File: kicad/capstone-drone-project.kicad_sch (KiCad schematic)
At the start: 0 parts

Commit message: update schematic
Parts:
- added C1, C2: C, symbol Device:C
- added Q1: PMOS, symbol Simulation_SPICE:PMOS
- added R1: 10k, symbol Device:R
- added U1: ESP32-S3, Package_DFN_QFN:QFN-56-1EP_7x7mm_P0.4mm_EP4x4mm, symbol MCU_Espressif:ESP32-S3
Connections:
- new net: Q1.3 (S), R1.1, U1.4 (CHIP_PU)
- new net EN: Q1.2 (G)
- new net GND: C1.2, C2.2, Q1.1 (D), R1.2, U1.57 (GND)
- new net Vcc: C1.1, C2.1, U1.2 (VDD3P3), U1.20 (VDD3P3_RTC), U1.29 (VDD_SPI), U1.3 (VDD3P3), U1.46 (VDD3P3_CPU), U1.55 (VDDA), U1.56 (VDDA)
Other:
- note added: "power supply undetermined but will need voltage regulator"

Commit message: update schematic
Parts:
- added L1: 24n, symbol Device:L
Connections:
- net at U1.54 (XTAL_P): now also L1.2
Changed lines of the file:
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@@
+	)
+	(symbol
+		(lib_id "Device:L")
+		(at 104.14 111.76 90)
+		(unit 1)
+		(exclude_from_sim no)
+		(in_bom yes)
+		(on_board yes)
+		(dnp no)
+		(property "Reference" "L1"
+			(at 104.14 106.68 90)
+			(effects
+				(font
+					(size 1.27 1.27)
+				)
+			)
+		)
+		(property "Value" "24n"
+			(at 104.14 109.22 90)
+			(effects
+				(font
+					(size 1.27 1.27)
+				)
+			)
+		)
+		(property "Footprint" ""
+			(at 104.14 111.76 0)
+			(effects
+				(font
+					(size 1.27 1.27)
+				)
+				(hide yes)
+			)
+		)
+		(property "Datasheet" "~"
+			(at 104.14 111.76 0)
+			(effects
+				(font
+					(size 1.27 1.27)
+				)
+				(hide yes)
+			)
+		)
+		(property "Description" "Inductor"
+			(at 104.14 111.76 0)
+			(effects
+				(font
+					(size 1.27 1.27)
+				)
+				(hide yes)
+			)
+		)
+		(pin "2"
+		)
+		(pin "1"
+		)
+		(instances
+			(project ""
+				(path "/99584293-ff2b-4397-8b8b-c39f1581dc82"
+					(reference "L1")
+					(unit 1)
+				)
+			)
+		)
 	)
 	(symbol

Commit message: working on external clock
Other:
- note added: "maybe use ~26pF capacitors with 18pF,40MHz crystal?"
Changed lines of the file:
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@@
+		)
+	)
+	(text "maybe use ~26pF capacitors with 18pF,40MHz crystal?"
+		(exclude_from_sim no)
+		(at 68.834 104.14 0)
+		(effects
+			(font
+				(size 1.27 1.27)
+			)
 		)
 	)

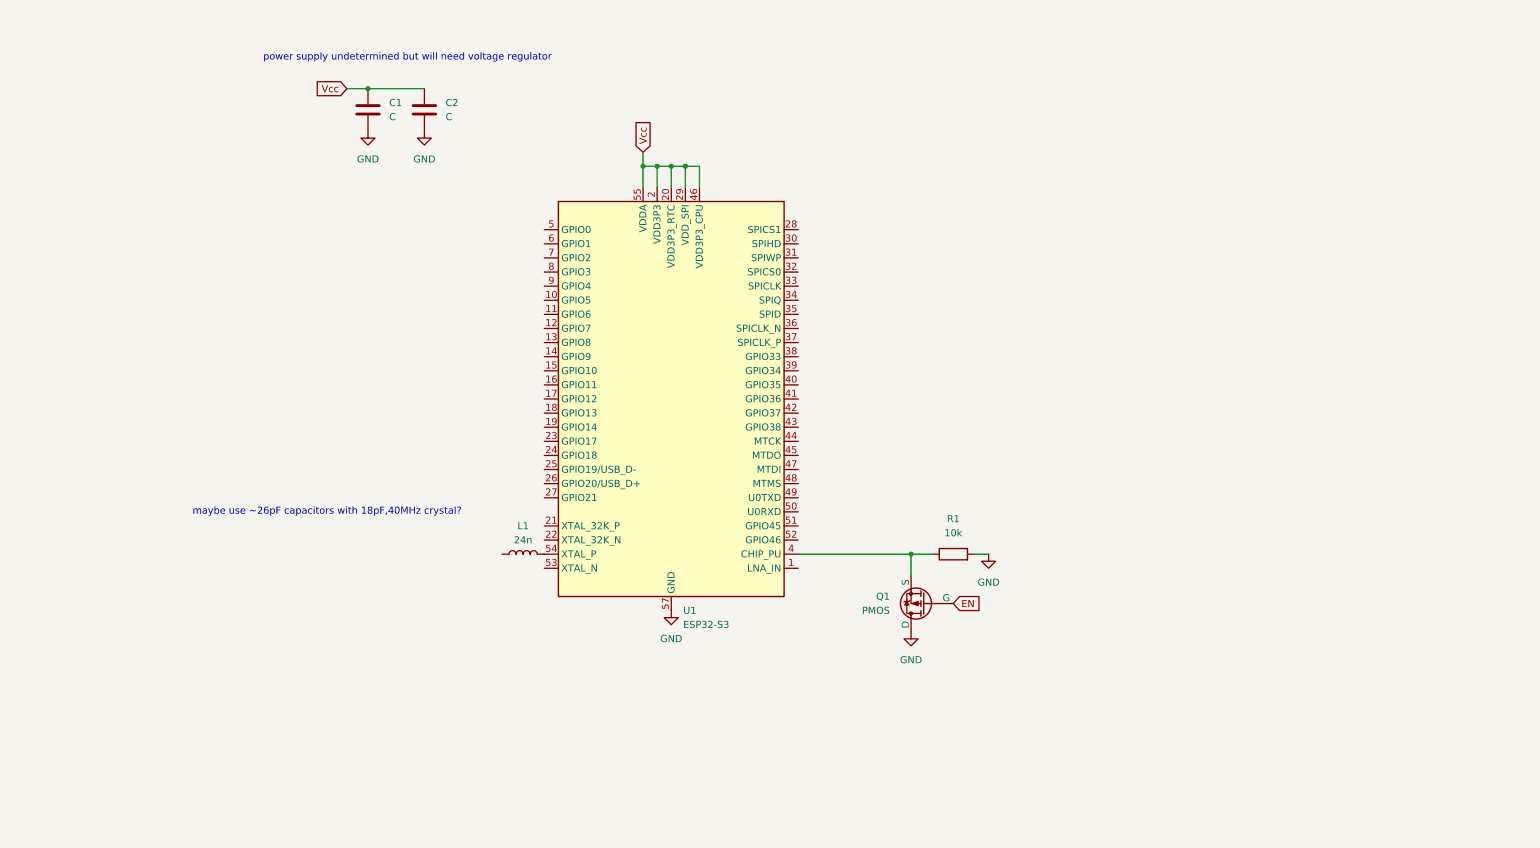
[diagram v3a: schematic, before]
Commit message: added required crystal oscillator and bypass caps
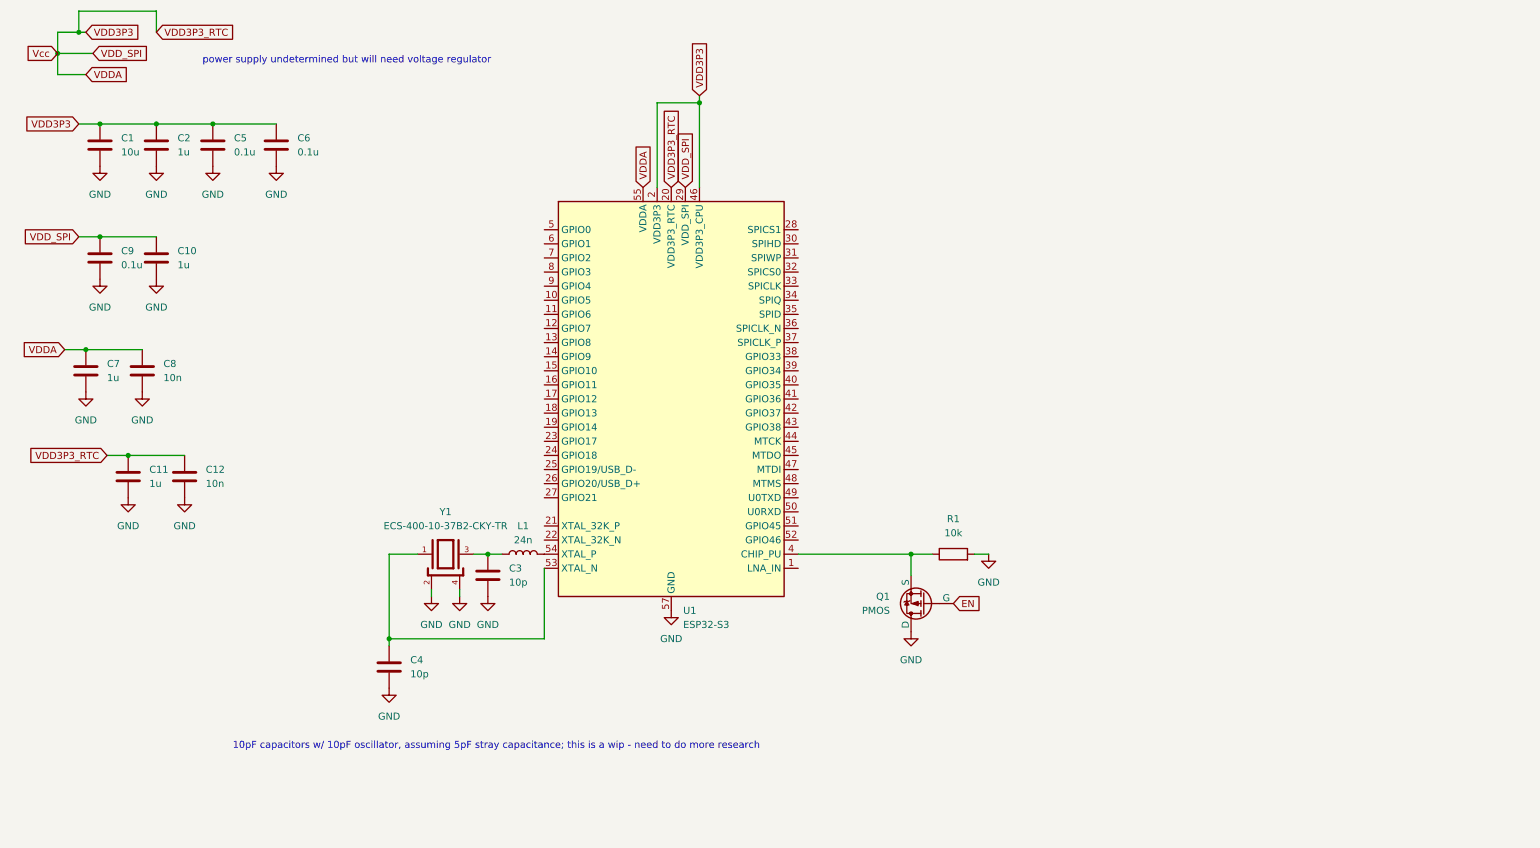
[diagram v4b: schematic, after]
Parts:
- added C10, C11, C7: 1u, symbol Device:C
- added C12, C8: 10n, symbol Device:C
- added C3, C4: 10p, symbol Device:C
- added C5, C6, C9: 0.1u, symbol Device:C
- added Y1: ECS-400-10-37B2-CKY-TR, ECS-400-10-37B2-CKY-TR:XTAL_ECS-400-10-37B2-CKY-TR, symbol ECS-400-10-37B2-CKY-TR:ECS-400-10-37B2-CKY-TR
- C1: value C -> 10u
- C2: value C -> 1u
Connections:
- net GND: now also C10.2, C11.2, C12.2, C3.2, C4.2, C5.2, C6.2, C7.2, C8.2, C9.2, Y1.2, Y1.4
- net at U1.53 (XTAL_N): now also C4.1, Y1.1
- net at L1.1: now also C3.1, Y1.3
- net Vcc renamed VDD3P3
- net VDD3P3: now also C10.1, C11.1, C12.1, C5.1, C6.1, C7.1, C8.1, C9.1
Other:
- note added: "10pF capacitors w/ 10pF oscillator, assuming 5pF stray capacitance; this is a wip - need to do more research"
- note removed: "maybe use ~26pF capacitors with 18pF,40MHz crystal?"
- moved on the sheet: C1, C2

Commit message: add strapping pins for boot mode
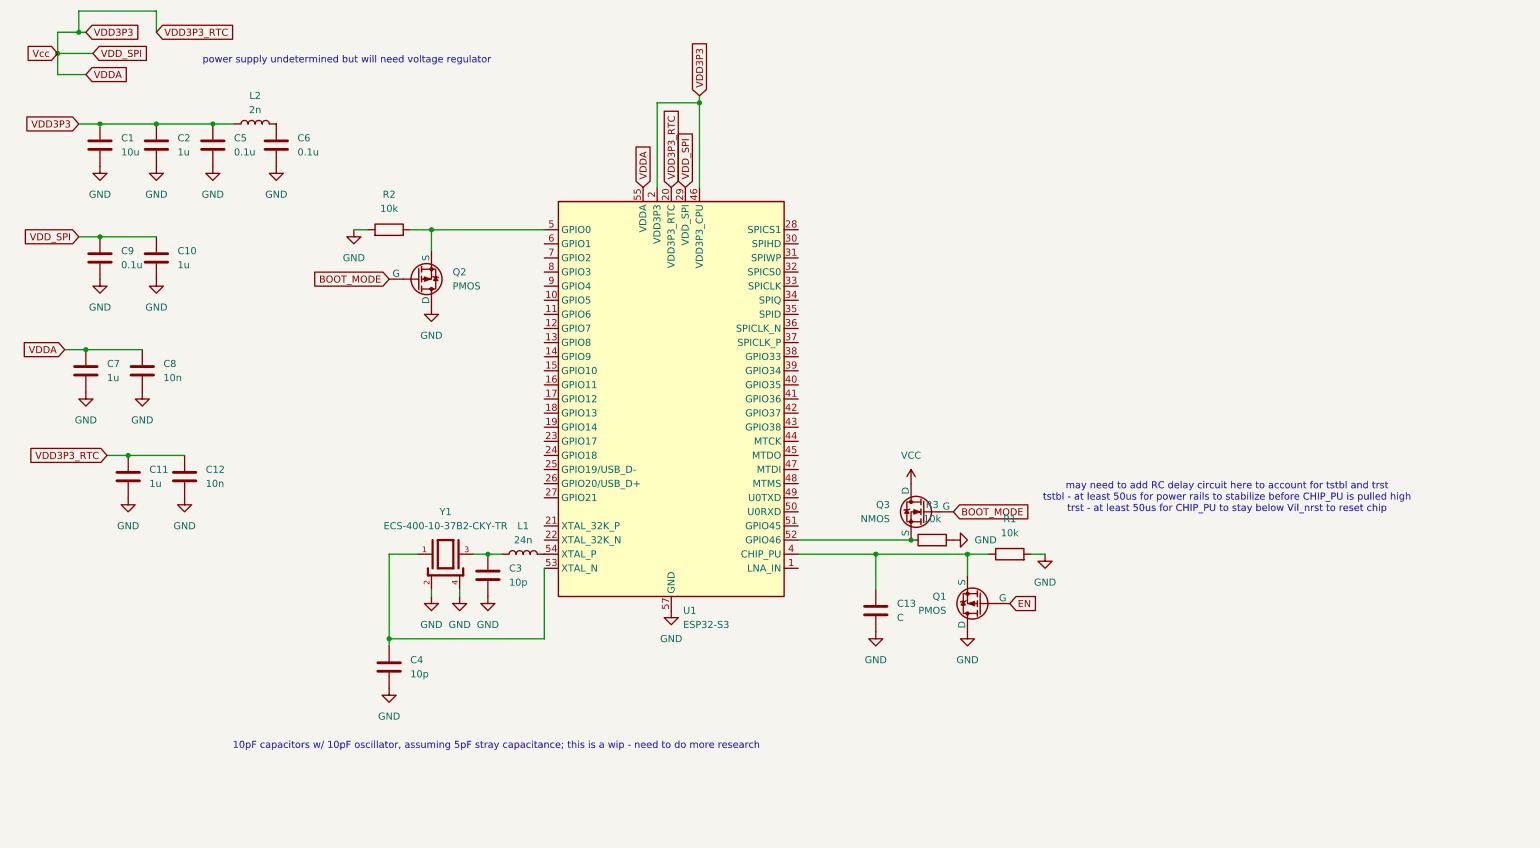
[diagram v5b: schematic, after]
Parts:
- added C13: C, symbol Device:C
- added L2: 2n, symbol Device:L
- added Q2: PMOS, symbol Simulation_SPICE:PMOS
- added Q3: NMOS, symbol Simulation_SPICE:NMOS
- added R2, R3: 10k, symbol Device:R
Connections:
- net GND: now also C13.2, Q2.1 (D), R2.2, R3.2
- net VDD3P3: now also L2.1; no longer C6.1
- net at Q1.3 (S), R1.1, U1.4 (CHIP_PU): now also C13.1
- net at U1.5 (GPIO0): now also Q2.3 (S), R2.1
- net at U1.52 (GPIO46): now also Q3.3 (S), R3.1
- new net: C6.1, L2.2
- new net BOOT_MODE: Q2.2 (G), Q3.2 (G)
- new net VCC: Q3.1 (D)
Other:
- note added: "may need to add RC delay circuit here to account for tstbl and trst tstbl - at least 50us for power rails to stabilize before CHIP_PU is pulled high trst - at least 50us for CHIP_PU to stay below Vil_nrst to reset chip"
- moved on the sheet: Q1, R1

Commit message: implementing psram
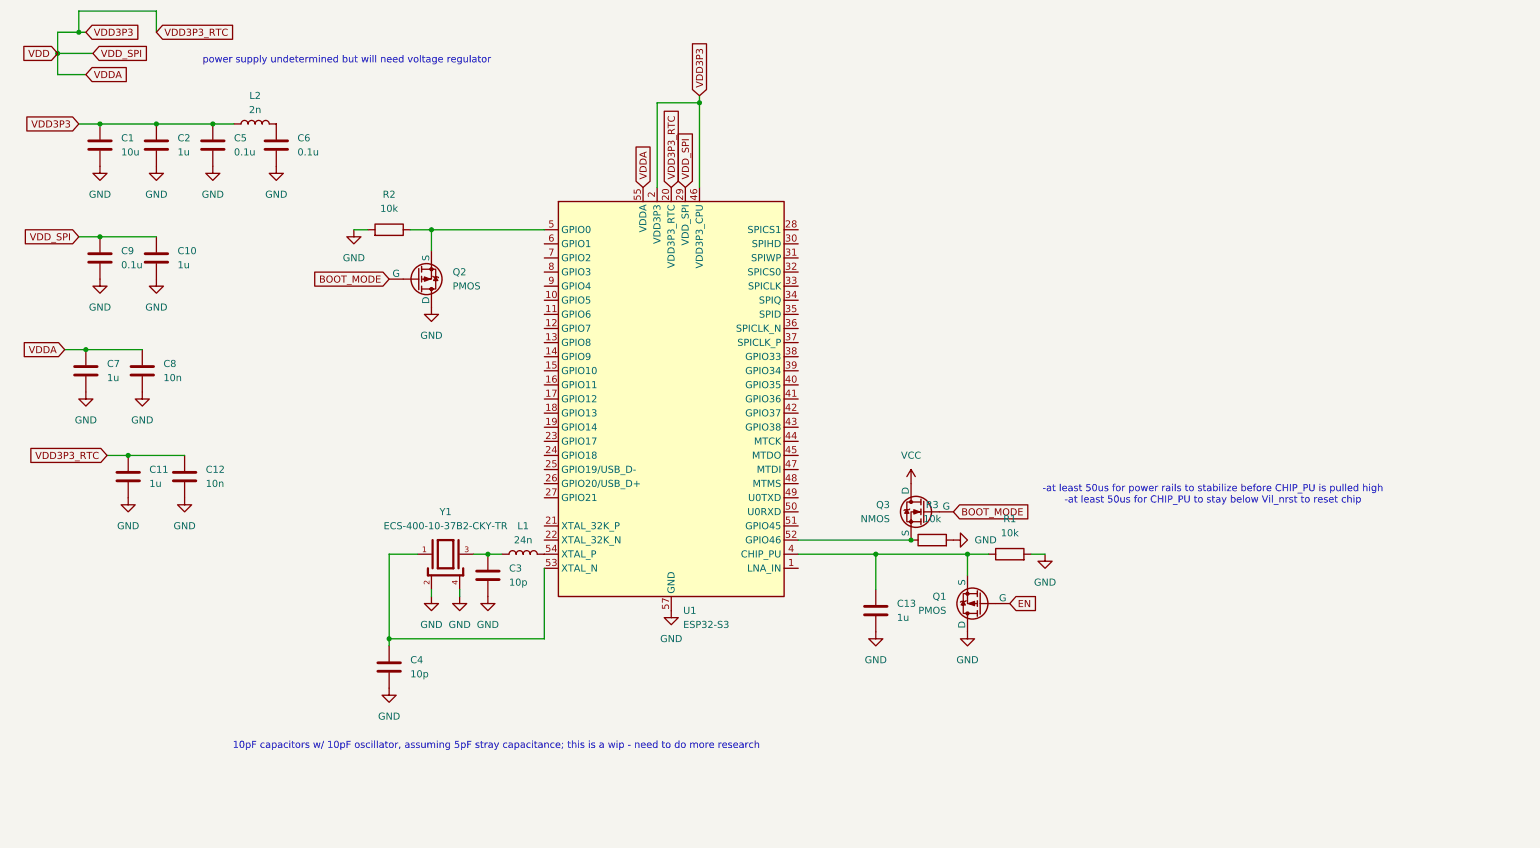
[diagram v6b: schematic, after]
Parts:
- C13: value C -> 1u
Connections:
- net VDD3P3 renamed VDD 
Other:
- note added: "-at least 50us for power rails to stabilize before CHIP_PU is pulled high -at least 50us for CHIP_PU to stay below Vil_nrst to reset chip"
- note removed: "may need to add RC delay circuit here to account for tstbl and trst tstbl - at least 50us for power rails to stabilize before CHIP_PU is pulled high trst - at least 50us for CHIP_PU to stay below Vil_nrst to reset chip"
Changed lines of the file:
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@@
 		)
 	)
-	(text "may need to add RC delay circuit here to account for tstbl and trst\ntstbl - at least 50us for power rails to stabilize before CHIP_PU is pulled high\ntrst - at least 50us for CHIP_PU to stay below Vil_nrst to reset chip"
+	(text "-at least 50us for power rails to stabilize before CHIP_PU is pulled high\n-at least 50us for CHIP_PU to stay below Vil_nrst to reset chip"
 		(exclude_from_sim no)
-		(at 230.886 101.6 0)
+		(at 228.346 101.092 0)
 		(effects
 			(font
@@
 		)
 	)
-	(global_label "Vcc"
+	(global_label "VDD "
 		(shape input)
 		(at 20.32 21.59 180)
@@
 		)
 		(property "Intersheetrefs" "${INTERSHEET_REFS}"
-			(at 14.069 21.59 0)
+			(at 12.7386 21.59 0)
 			(effects
 				(font
@@
 			)
 		)
-		(property "Value" "C"
+		(property "Value" "1u"
 			(at 171.45 123.1899 0)
 			(effects

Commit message: added psram
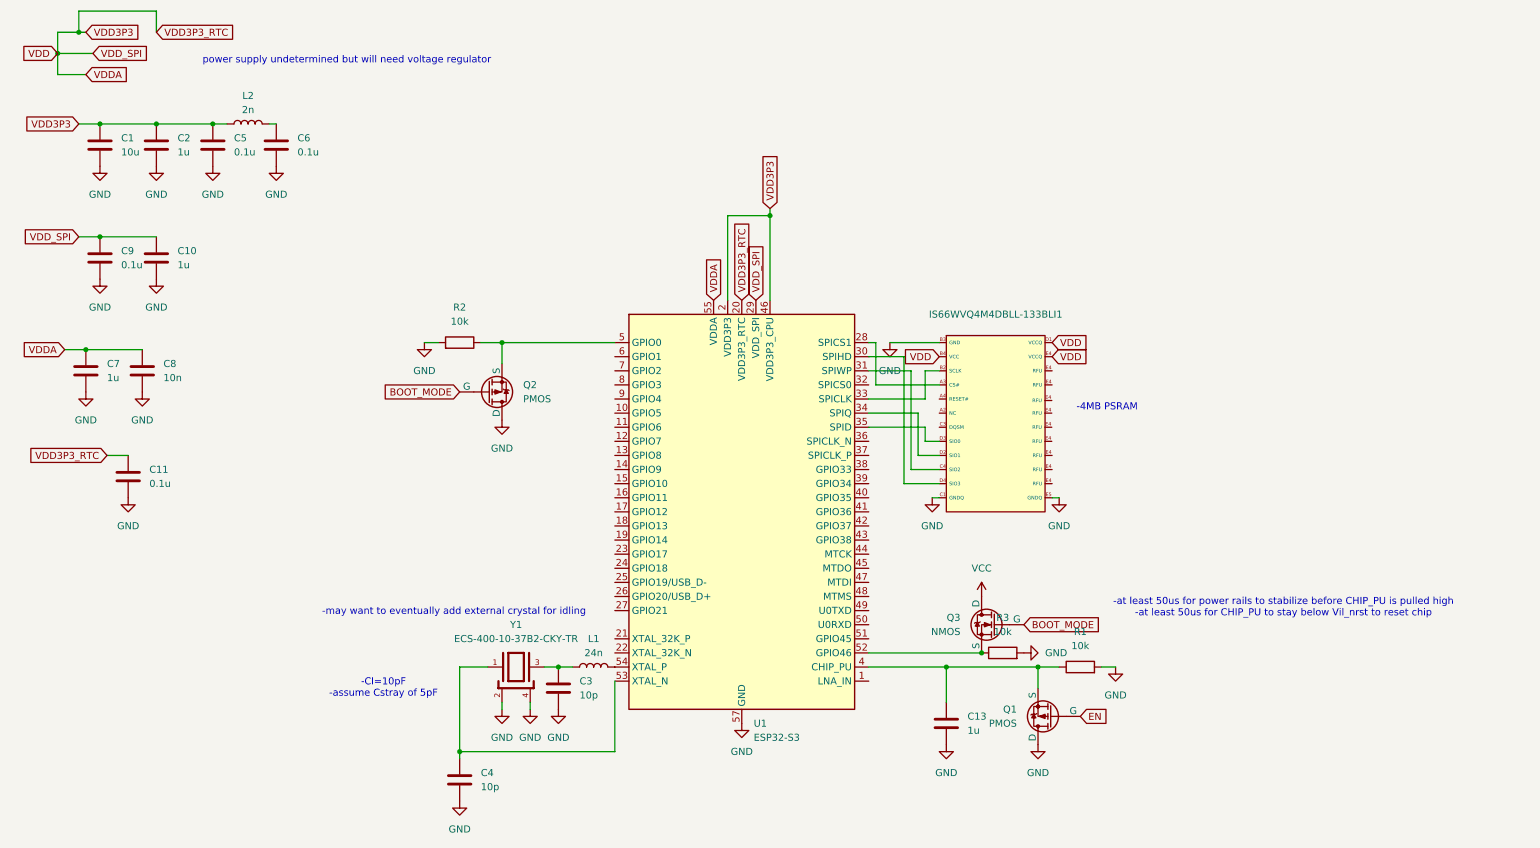
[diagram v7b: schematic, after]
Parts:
- removed C12: 10n, symbol Device:C
- added IS66WVQ4M4DBLL-133BLI1: ~, symbol capstone-drone-project-library:IS66WVQ4M4DBLL-133BLI
- C11: value 1u -> 0.1u
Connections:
- net GND: now also IS66WVQ4M4DBLL-133BLI1.B3 (GND), IS66WVQ4M4DBLL-133BLI1.C1 (GNDQ), IS66WVQ4M4DBLL-133BLI1.E5 (GNDQ)
- net VDD : now also IS66WVQ4M4DBLL-133BLI1.B4 (VCC), IS66WVQ4M4DBLL-133BLI1.D1 (VCCQ), IS66WVQ4M4DBLL-133BLI1.E4 (RFU)
- net at U1.28 (SPICS1): now also IS66WVQ4M4DBLL-133BLI1.A3 (CS#)
- net at U1.30 (SPIHD): now also IS66WVQ4M4DBLL-133BLI1.D4 (SIO3)
- net at U1.31 (SPIWP): now also IS66WVQ4M4DBLL-133BLI1.C4 (SIO2)
- net at U1.33 (SPICLK): now also IS66WVQ4M4DBLL-133BLI1.B2 (SCLK)
- net at U1.34 (SPIQ): now also IS66WVQ4M4DBLL-133BLI1.D2 (SIO1)
- net at U1.35 (SPID): now also IS66WVQ4M4DBLL-133BLI1.D3 (SIO0)
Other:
- note added: "-4MB PSRAM"
- note added: "-Cl=10pF -assume Cstray of 5pF"
- note added: "-may want to eventually add external crystal for idling"
- note removed: "10pF capacitors w/ 10pF oscillator, assuming 5pF stray capacitance; this is a wip - need to do more research"
- moved on the sheet: C13, C3, C4, L1, L2, Q1, Q2, Q3, R1, R2, R3, U1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
